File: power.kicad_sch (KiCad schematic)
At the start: 41 parts, among them U33001 MC7805

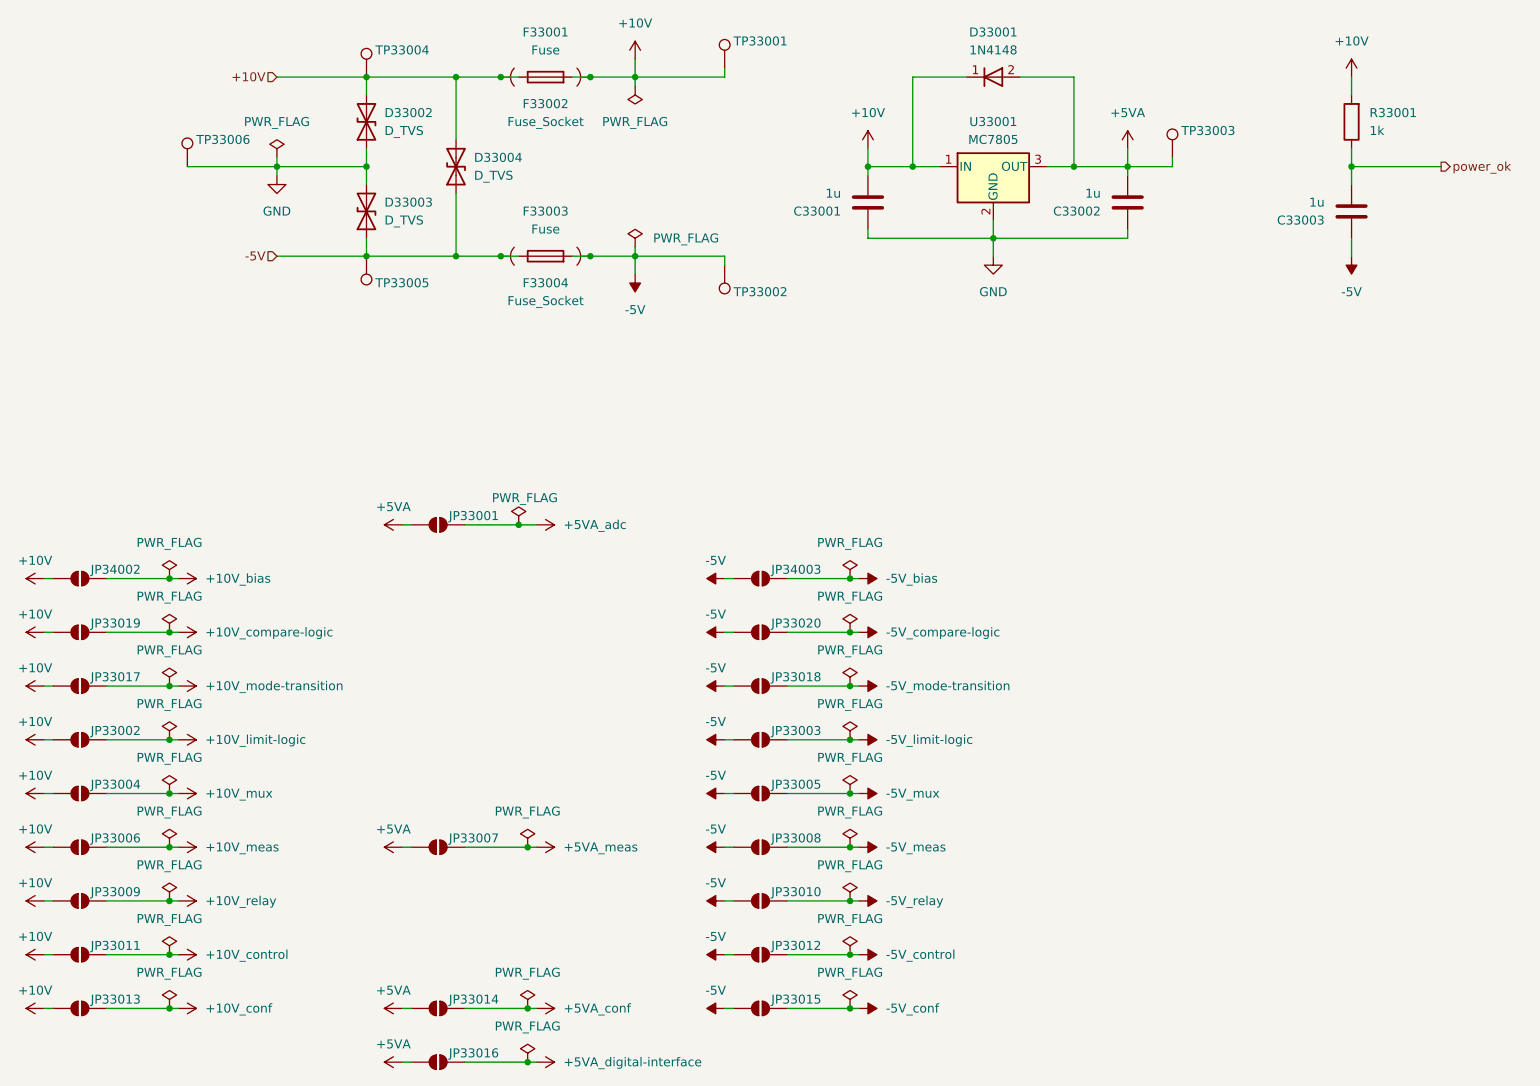
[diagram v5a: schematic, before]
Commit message: edit pss footprint library: export all footprints to library 'pss' and update footprint links
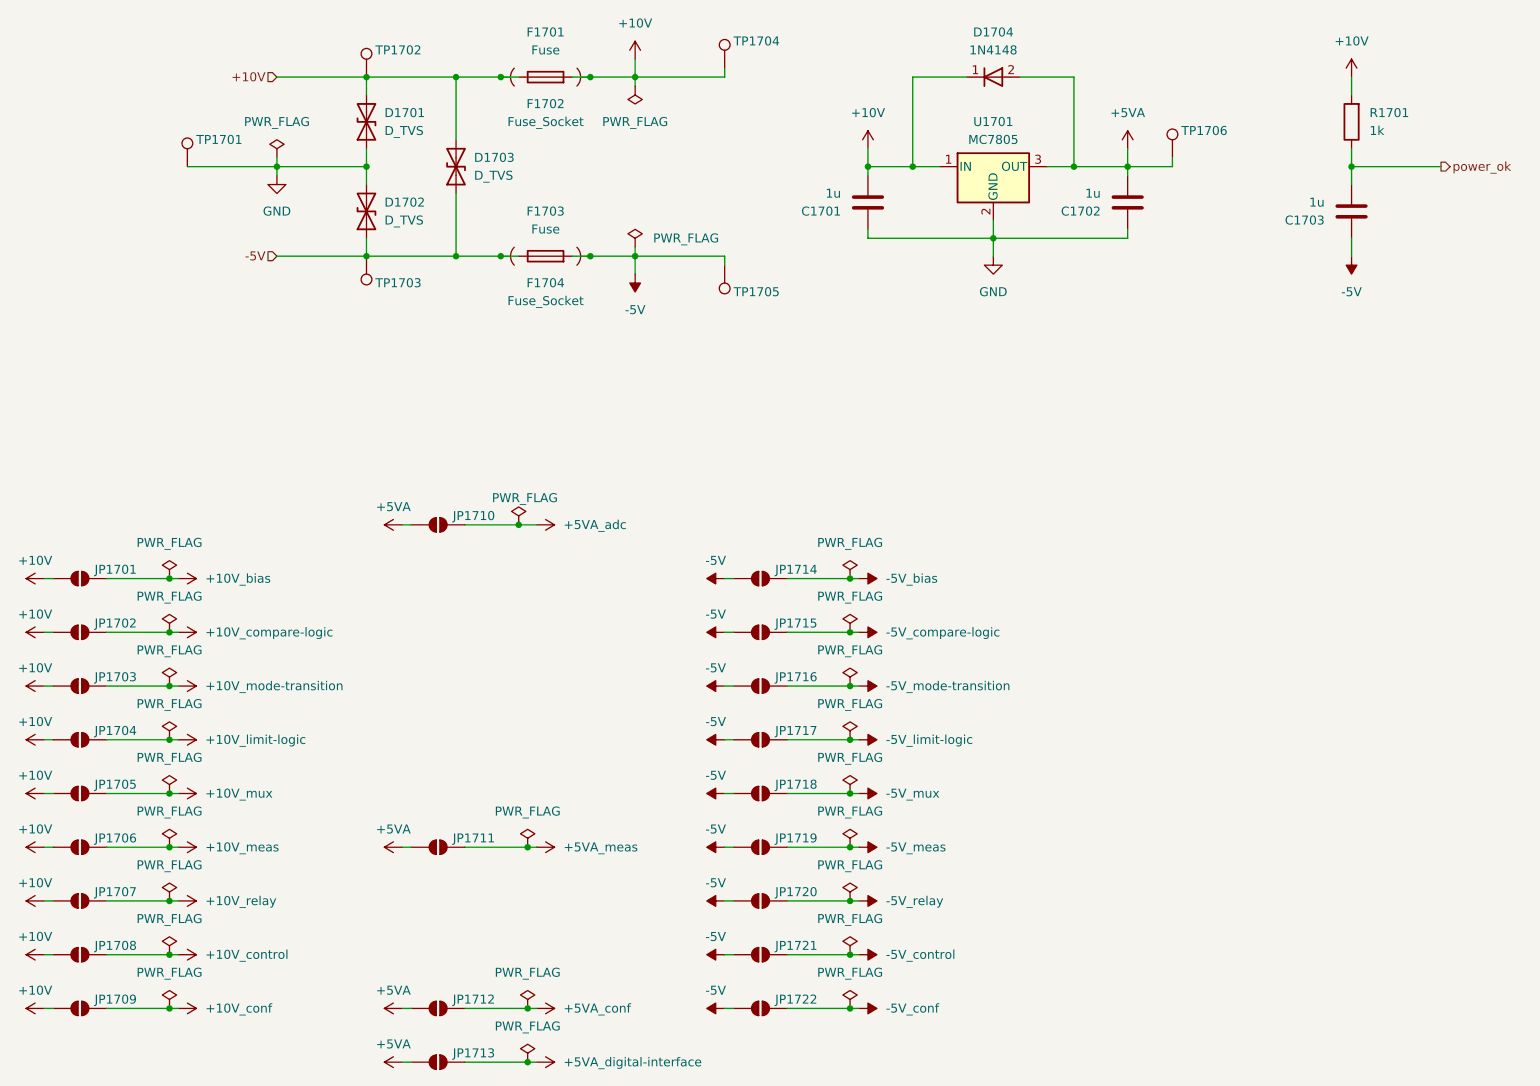
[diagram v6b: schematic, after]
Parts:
- C1701: renamed from C33001; footprint Capacitor_SMD:C_0603_1608Metric_Pad1.08x0.95mm_HandSolder -> pss:C_0603_1608Metric_Pad1.08x0.95mm_HandSolder
- C1702: renamed from C33002; footprint Capacitor_SMD:C_0603_1608Metric_Pad1.08x0.95mm_HandSolder -> pss:C_0603_1608Metric_Pad1.08x0.95mm_HandSolder
- C1703: renamed from C33003; footprint Capacitor_SMD:C_0603_1608Metric_Pad1.08x0.95mm_HandSolder -> pss:C_0603_1608Metric_Pad1.08x0.95mm_HandSolder
- D1701: renamed from D33002; footprint Diode_SMD:D_SOD-323_HandSoldering -> pss:D_SOD-323_HandSoldering
- D1702: renamed from D33003; footprint Diode_SMD:D_SOD-323_HandSoldering -> pss:D_SOD-323_HandSoldering
- D1703: renamed from D33004; footprint Diode_SMD:D_SOD-323_HandSoldering -> pss:D_SOD-323_HandSoldering
- D1704: renamed from D33001; footprint Diode_SMD:D_SOD-123 -> pss:D_SOD-123
- JP1701: renamed from JP34002; footprint Jumper:SolderJumper-2_P1.3mm_Open_RoundedPad1.0x1.5mm -> pss:SolderJumper-2_P1.3mm_Open_RoundedPad1.0x1.5mm
- JP1702: renamed from JP33019; footprint Jumper:SolderJumper-2_P1.3mm_Open_RoundedPad1.0x1.5mm -> pss:SolderJumper-2_P1.3mm_Open_RoundedPad1.0x1.5mm
- JP1703: renamed from JP33017; footprint Jumper:SolderJumper-2_P1.3mm_Open_RoundedPad1.0x1.5mm -> pss:SolderJumper-2_P1.3mm_Open_RoundedPad1.0x1.5mm
- JP1704: renamed from JP33002; footprint Jumper:SolderJumper-2_P1.3mm_Open_RoundedPad1.0x1.5mm -> pss:SolderJumper-2_P1.3mm_Open_RoundedPad1.0x1.5mm
- JP1705: renamed from JP33004; footprint Jumper:SolderJumper-2_P1.3mm_Open_RoundedPad1.0x1.5mm -> pss:SolderJumper-2_P1.3mm_Open_RoundedPad1.0x1.5mm
- JP1706: renamed from JP33006; footprint Jumper:SolderJumper-2_P1.3mm_Open_RoundedPad1.0x1.5mm -> pss:SolderJumper-2_P1.3mm_Open_RoundedPad1.0x1.5mm
- JP1707: renamed from JP33009; footprint Jumper:SolderJumper-2_P1.3mm_Open_RoundedPad1.0x1.5mm -> pss:SolderJumper-2_P1.3mm_Open_RoundedPad1.0x1.5mm
- JP1708: renamed from JP33011; footprint Jumper:SolderJumper-2_P1.3mm_Open_RoundedPad1.0x1.5mm -> pss:SolderJumper-2_P1.3mm_Open_RoundedPad1.0x1.5mm
- JP1709: renamed from JP33013; footprint Jumper:SolderJumper-2_P1.3mm_Open_RoundedPad1.0x1.5mm -> pss:SolderJumper-2_P1.3mm_Open_RoundedPad1.0x1.5mm
- JP1710: renamed from JP33001; footprint Jumper:SolderJumper-2_P1.3mm_Open_RoundedPad1.0x1.5mm -> pss:SolderJumper-2_P1.3mm_Open_RoundedPad1.0x1.5mm
- JP1711: renamed from JP33007; footprint Jumper:SolderJumper-2_P1.3mm_Open_RoundedPad1.0x1.5mm -> pss:SolderJumper-2_P1.3mm_Open_RoundedPad1.0x1.5mm
- JP1712: renamed from JP33014; footprint Jumper:SolderJumper-2_P1.3mm_Open_RoundedPad1.0x1.5mm -> pss:SolderJumper-2_P1.3mm_Open_RoundedPad1.0x1.5mm
- JP1713: renamed from JP33016; footprint Jumper:SolderJumper-2_P1.3mm_Open_RoundedPad1.0x1.5mm -> pss:SolderJumper-2_P1.3mm_Open_RoundedPad1.0x1.5mm
- JP1714: renamed from JP34003; footprint Jumper:SolderJumper-2_P1.3mm_Open_RoundedPad1.0x1.5mm -> pss:SolderJumper-2_P1.3mm_Open_RoundedPad1.0x1.5mm
- JP1715: renamed from JP33020; footprint Jumper:SolderJumper-2_P1.3mm_Open_RoundedPad1.0x1.5mm -> pss:SolderJumper-2_P1.3mm_Open_RoundedPad1.0x1.5mm
- JP1716: renamed from JP33018; footprint Jumper:SolderJumper-2_P1.3mm_Open_RoundedPad1.0x1.5mm -> pss:SolderJumper-2_P1.3mm_Open_RoundedPad1.0x1.5mm
- JP1717: renamed from JP33003; footprint Jumper:SolderJumper-2_P1.3mm_Open_RoundedPad1.0x1.5mm -> pss:SolderJumper-2_P1.3mm_Open_RoundedPad1.0x1.5mm
- JP1718: renamed from JP33005; footprint Jumper:SolderJumper-2_P1.3mm_Open_RoundedPad1.0x1.5mm -> pss:SolderJumper-2_P1.3mm_Open_RoundedPad1.0x1.5mm
- JP1719: renamed from JP33008; footprint Jumper:SolderJumper-2_P1.3mm_Open_RoundedPad1.0x1.5mm -> pss:SolderJumper-2_P1.3mm_Open_RoundedPad1.0x1.5mm
- JP1720: renamed from JP33010; footprint Jumper:SolderJumper-2_P1.3mm_Open_RoundedPad1.0x1.5mm -> pss:SolderJumper-2_P1.3mm_Open_RoundedPad1.0x1.5mm
- JP1721: renamed from JP33012; footprint Jumper:SolderJumper-2_P1.3mm_Open_RoundedPad1.0x1.5mm -> pss:SolderJumper-2_P1.3mm_Open_RoundedPad1.0x1.5mm
- JP1722: renamed from JP33015; footprint Jumper:SolderJumper-2_P1.3mm_Open_RoundedPad1.0x1.5mm -> pss:SolderJumper-2_P1.3mm_Open_RoundedPad1.0x1.5mm
- R1701: renamed from R33001; footprint Resistor_SMD:R_1210_3225Metric_Pad1.30x2.65mm_HandSolder -> pss:R_1210_3225Metric_Pad1.30x2.65mm_HandSolder
- U1701: renamed from U33001; footprint Package_TO_SOT_SMD:TO-252-2 -> pss:TO-252-2
- renumbered F33001 to F1701, F33002 to F1702, F33003 to F1703, F33004 to F1704, TP33006 to TP1701, TP33004 to TP1702, TP33005 to TP1703, TP33001 to TP1704, TP33002 to TP1705, TP33003 to TP1706
